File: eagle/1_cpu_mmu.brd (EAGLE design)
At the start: 30 parts, among them IC1 MT5C6408, IC10 74LS157N, IC11 74LS157N, IC12 74LS157N, IC13 74LS157N, IC14 74LS157N, IC15 74LS04N, IC17 74LS32N, IC18 74LS00N, IC19 74LS32N, IC2 MT5C6408, IC20 74LS02N, IC21 74LS374N, IC3 74LS27N, IC4 74LS20N, IC5 74LS08N, IC6 74LS245N, IC7 74LS245N, IC8 74LS32N, IC9 74LS157N

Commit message: Sat Feb  6 20:10:54 CET 2016
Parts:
- removed IC12: 74LS157N, 74xx-eu:DIL16
- added IC16: 74LS08N, 74xx-eu:DIL14
- moved IC7 7.63 mm to (128.3, 40.3)
- moved IC2 1.27 mm to (114.0, 35.2)
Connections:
- removed net /ENMEMX: IC12.4
- removed net /LDMEMX: IC12.7
- removed net N$20: IC12.6, IC17.8
- removed net N$33: IC17.10, IC18.3
- removed net N$39: IC12.1, IC5.8
- new net N$3: IC16.12, IC20.4
- new net N$36: IC16.13, IC5.11
- new net N$38: IC16.11, IC4.13
- net +5V: no longer IC12.11, IC12.14, IC12.2, IC12.5
- net /ENMEM: no longer IC12.3
- net /LDMEM: no longer IC17.9
- net /NP_FAULT: no longer IC12.12
- net /PPREG: no longer IC5.10
- net /PTAB: no longer IC5.9
- net /WR_FAULT: no longer IC12.9
- net ABUS5: now also IC5.12
- net BUSCLKA: now also IC19.9
- net CLK0A: no longer IC19.9
- net GND: now also IC16.7; no longer IC12.15, IC12.8
- net MEMSEG: now also IC5.13
- net N$31: no longer IC12.10
- net N$32: no longer IC12.13
- net N$34: no longer IC18.2
- net N$35: no longer IC18.1
- net VCC: now also IC16.14; no longer IC12.16
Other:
- board text added: "#1"
- board text removed: "#0a"

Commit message: MMU board in progress
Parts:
- removed IC16: 74LS08N, 74xx-eu:DIL14
- removed IC17: 74LS32N, 74xx-eu:DIL14
- removed IC18: 74LS00N, 74xx-eu:DIL14
- added IC12: 74LS00N, 74xx-eu:DIL14
- JP5: device pinhead:2X05 -> pinhead:2X06
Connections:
- removed net N$34: IC17.11, IC17.4
- removed net N$35: IC17.1, IC19.3
- new net /ENMEMX: JP5.11
- new net /LDMEMX: JP5.12
- new net /MEMOP: IC19.1, JP10.11
- new net N$20: IC19.3, IC19.4
- net /ENMEM: no longer IC5.5
- net /FP: no longer IC17.13
- net /LDMEM: no longer IC17.5, IC5.4
- net /PPREG: now also IC12.10
- net /PTAB: now also IC12.9
- net FPRESENT: no longer IC19.1
- net FWRITABLE: no longer IC17.12
- net GND: now also IC12.7; no longer IC16.7, IC17.7, IC18.7
- net N$19: now also IC12.2; no longer IC17.2, IC5.6
- net N$3: now also IC5.9; no longer IC16.12
- net N$31: now also IC12.1; no longer IC17.6, IC18.9
- net N$32: now also IC12.8, IC19.5; no longer IC17.3, IC18.10
- net N$36: now also IC5.10; no longer IC16.13
- net N$38: now also IC5.8; no longer IC16.11
- net N$40: now also IC12.3; no longer IC18.8
- net VCC: now also IC12.14; no longer IC16.14, IC17.14, IC18.14

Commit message: MMU schematics completed
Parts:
- removed IC15: 74LS04N, 74xx-eu:DIL14
- added IC16: 74LS08N, 74xx-eu:DIL14
- added IC17: 74LS32N, 74xx-eu:DIL14
- moved IC3 115.5 mm to (119.4, 17.8), turned to 180 degrees
- moved IC12 107.1 mm to (41.3, 84.8), turned to 270 degrees
- moved IC4 86.7 mm to (91.1, 17.8)
- moved IC9 74.7 mm to (117.8, 45.1), turned to 180 degrees
- moved IC2 69.1 mm to (58.1, 75.9)
- moved IC19 68.3 mm to (23.2, 72.1), turned to 270 degrees
- moved IC5 62.9 mm to (68.6, 17.8)
- moved IC13 61.7 mm to (117.8, 31.4), turned to 180 degrees
- moved IC10 45.6 mm to (89.9, 45.1), turned to 180 degrees
- moved IC7 44.9 mm to (109.9, 81.3)
- moved IC21 43.8 mm to (92.4, 70.8), turned to 90 degrees
- moved IC20 43.7 mm to (44.8, 31.8)
- moved IC1 38.7 mm to (75.2, 75.9)
- moved IC14 33.1 mm to (89.9, 31.4), turned to 180 degrees
- moved IC11 21.0 mm to (64.1, 45.1), turned to 180 degrees
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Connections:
- removed net FIO: IC15.3, IC2.17, IC7.7
- removed net FPRESENT: IC2.19, IC7.9
- removed net FWRITABLE: IC2.18, IC7.8
- removed net N$18: IC11.11, IC15.4
- removed net N$19: IC12.2
- removed net N$31: IC12.1
- new net /FIO: IC11.11, IC2.17, IC7.7
- new net /FPRESENT: IC12.4, IC2.19, IC7.9
- new net /FWRITABLE: IC12.12, IC2.18, IC7.8
- new net N$33: IC12.5, IC20.1, IC5.4
- new net N$34: IC12.13, IC5.6
- net /ENMEM: now also IC17.2, IC5.5
- net /ENMEMX: now also IC17.3
- net /FP: now also IC17.10; no longer IC19.2
- net /LDMEM: now also IC17.5
- net /LDMEMX: now also IC17.6
- net /MEMOP: now also IC17.9; no longer IC19.1
- net /NP_FAULT: now also IC12.6, IC16.4
- net /WR_FAULT: now also IC12.11, IC16.5
- net ABUS0: now also IC12.2; no longer IC15.1
- net GND: now also IC16.7, IC17.7; no longer IC10.6, IC15.7
- net MEMSEG: now also IC10.6
- net N$20: now also IC17.8, IC20.2; no longer IC19.3, IC19.4
- net N$30: now also IC12.3; no longer IC15.2
- net N$32: now also IC17.1, IC17.4, IC20.3; no longer IC19.5
- net N$40: now also IC16.6; no longer IC12.3
- net VCC: now also IC16.14, IC17.14; no longer IC15.14
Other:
- board outline added: 160 x 100 mm

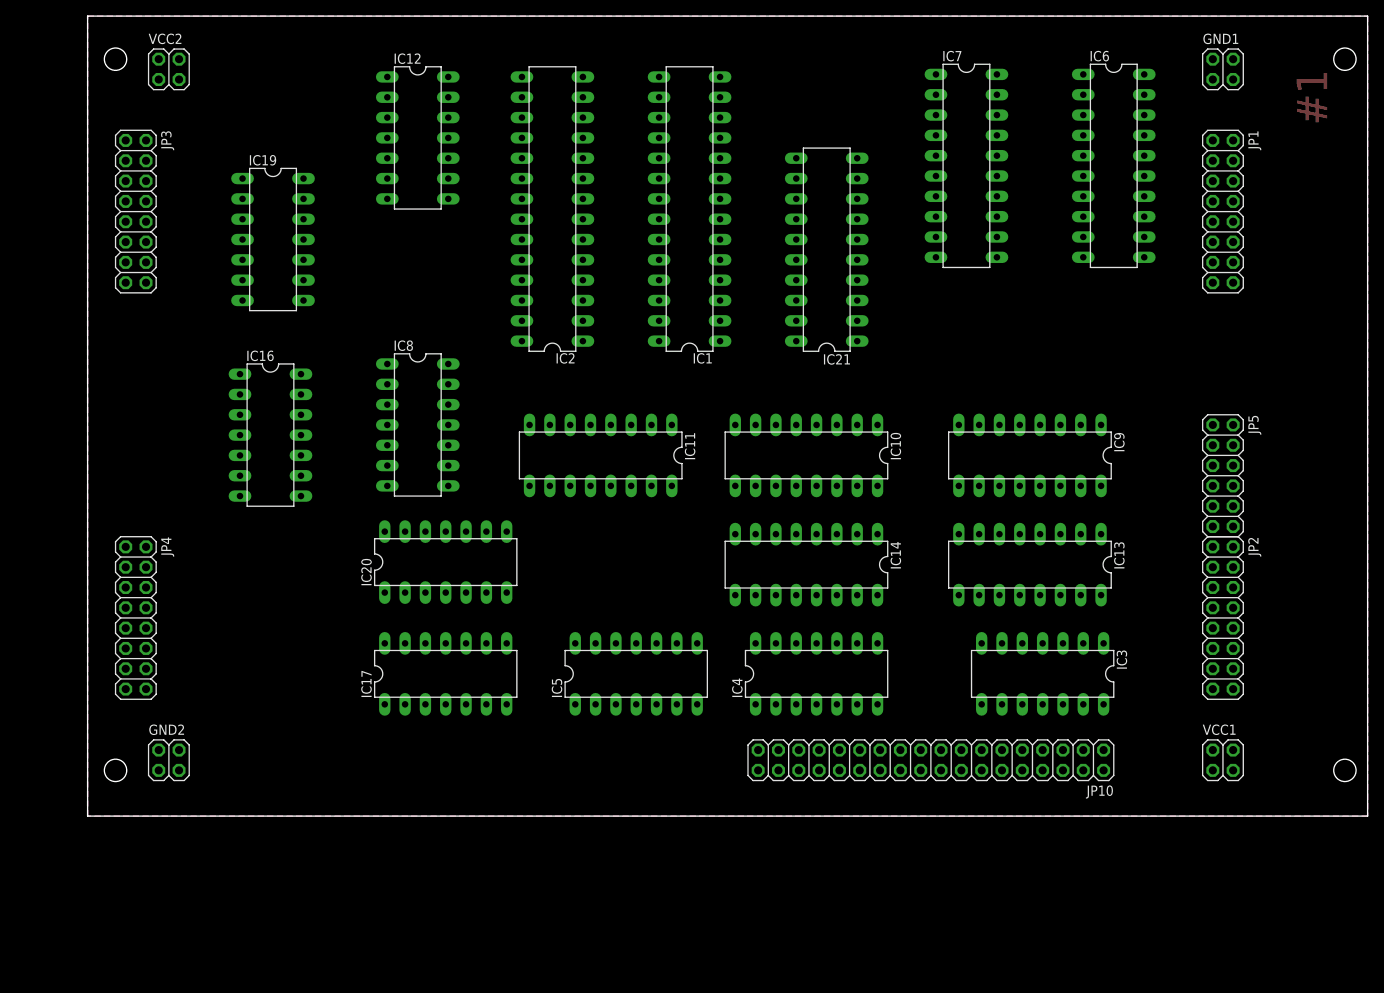
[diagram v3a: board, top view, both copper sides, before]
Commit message: MMU power rails and bypass caps added in schematic, board started
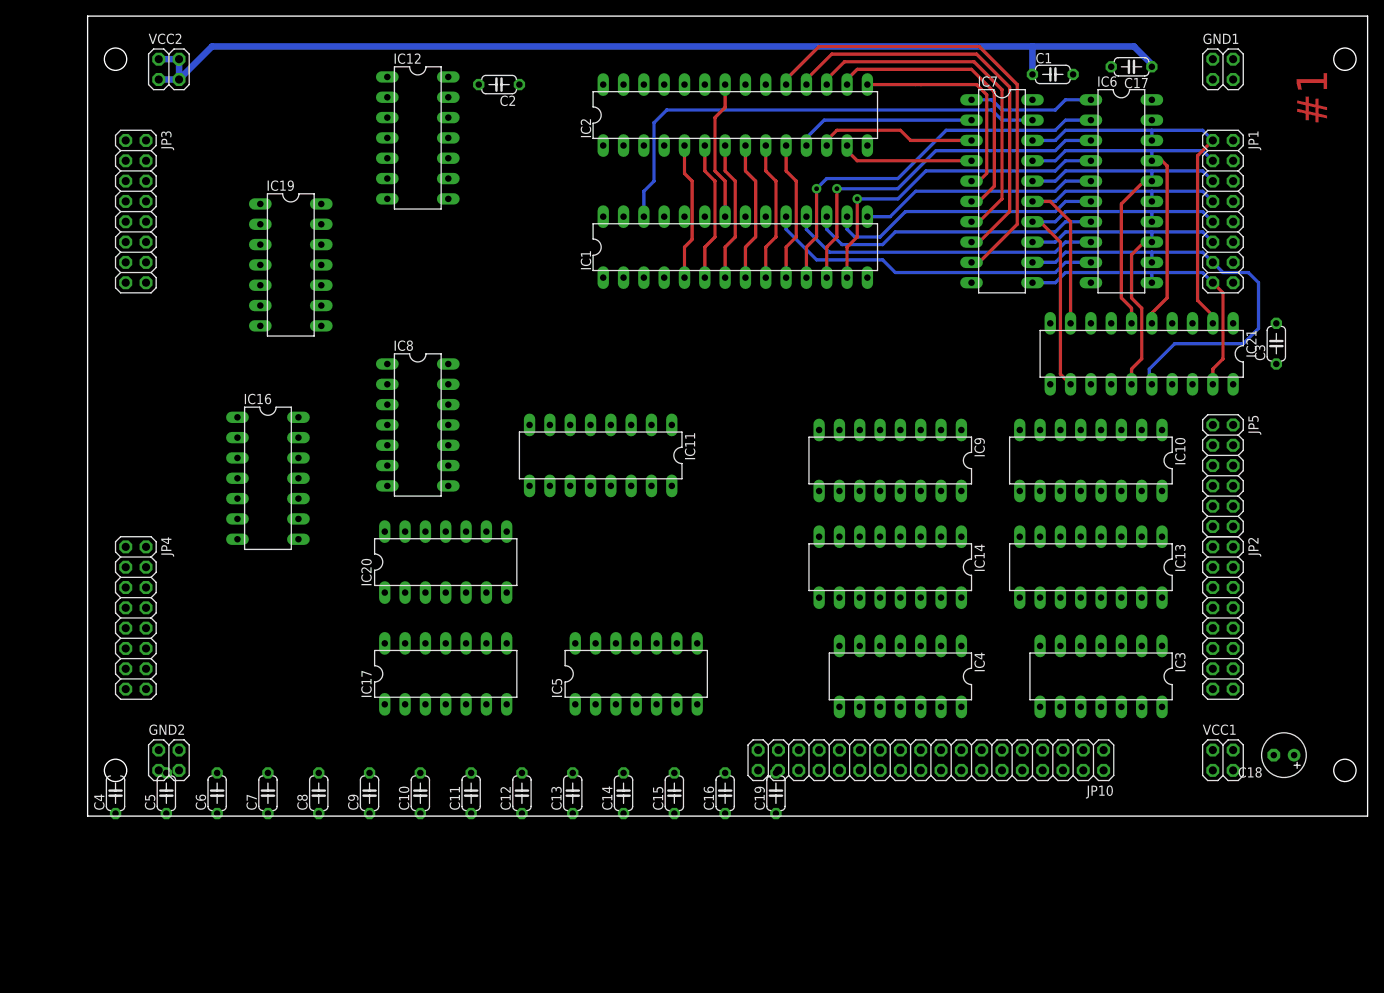
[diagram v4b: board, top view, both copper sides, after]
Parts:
- added C1, C10, C11, C12, C13, C14, C15, C16, C17, C19, C2, C3, C4, C5, C6, C7, C8, C9: 100n, rcl:C050-024X044
- added C18: 10u, rcl:E2,5-6
- moved IC21 41.5 mm to (131.8, 57.8), turned to 180 degrees
- moved IC10 35.6 mm to (125.4, 44.5)
- moved IC2 25.7 mm to (81.0, 87.6), turned to 0 degrees
- moved IC9 17.5 mm to (100.3, 44.5)
- moved IC14 10.5 mm to (100.3, 31.1)
- moved IC4 10.5 mm to (101.6, 17.5), turned to 180 degrees
- moved IC13 7.63 mm to (125.4, 31.1)
- moved IC1 7.44 mm to (81.0, 71.1), turned to 0 degrees
- moved IC3 7.31 mm to (126.7, 17.5)
- moved IC7 5.46 mm to (114.3, 78.1)
- moved IC16 5.41 mm to (22.5, 42.2)
- moved IC19 3.88 mm to (25.4, 68.9)
- moved IC6 3.31 mm to (129.2, 78.1)
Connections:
- net +5V: now also C1.1, C10.1, C11.1, C12.1, C13.1, C14.1, C15.1, C16.1, C17.1, C18.+, C19.1, C2.1, C3.1, C4.1, C5.1, C6.1, C7.1, C8.1, C9.1, IC1.28, IC10.16, IC11.16, IC12.14, IC13.16, IC14.16, IC16.14, IC17.14, IC19.14, IC2.28, IC20.14, IC21.20, IC3.14, IC4.14, IC5.14, IC6.20, IC7.20, IC9.16
- net GND: now also C1.2, C10.2, C11.2, C12.2, C13.2, C14.2, C15.2, C16.2, C17.2, C18.-, C19.2, C2.2, C3.2, C4.2, C5.2, C6.2, C7.2, C8.2, C9.2, IC16.1, IC16.10, IC16.12, IC16.13, IC16.2, IC16.9, IC17.12, IC17.13, IC19.1, IC19.2, IC19.4, IC19.5, IC20.11, IC20.12, IC20.8, IC20.9
- net VCC: no longer IC1.28, IC10.16, IC11.16, IC12.14, IC13.16, IC14.16, IC16.14, IC17.14, IC19.14, IC2.28, IC20.14, IC21.20, IC3.14, IC4.14, IC5.14, IC6.20, IC7.20, IC9.16
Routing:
- net +5V: track 0.00 -> 135.7 mm
- net N$27: track 0.00 -> 60.8 mm
- net /FPRESENT: track 0.00 -> 58.4 mm
- net DBUS6: track 0.00 -> 55.1 mm
- net /FWRITABLE: track 0.00 -> 51.0 mm
- net N$5: track 0.00 -> 49.5 mm, vias 0 -> 1
- net DBUS0: track 0.00 -> 49.3 mm
- net DBUS4: track 0.00 -> 47.7 mm
- net DBUS1: track 0.00 -> 47.5 mm
- net N$6: track 0.00 -> 45.9 mm, vias 0 -> 1
- net DBUS2: track 0.00 -> 45.3 mm
- net DBUS5: track 0.00 -> 45.3 mm
- net /FIO: track 0.00 -> 43.6 mm
- net DBUS3: track 0.00 -> 43.4 mm
- net N$12: track 0.00 -> 42.4 mm
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- removed copper zone on layer 1, net GND
- removed copper zone on layer 16, net GND

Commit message: MMU board layout updates
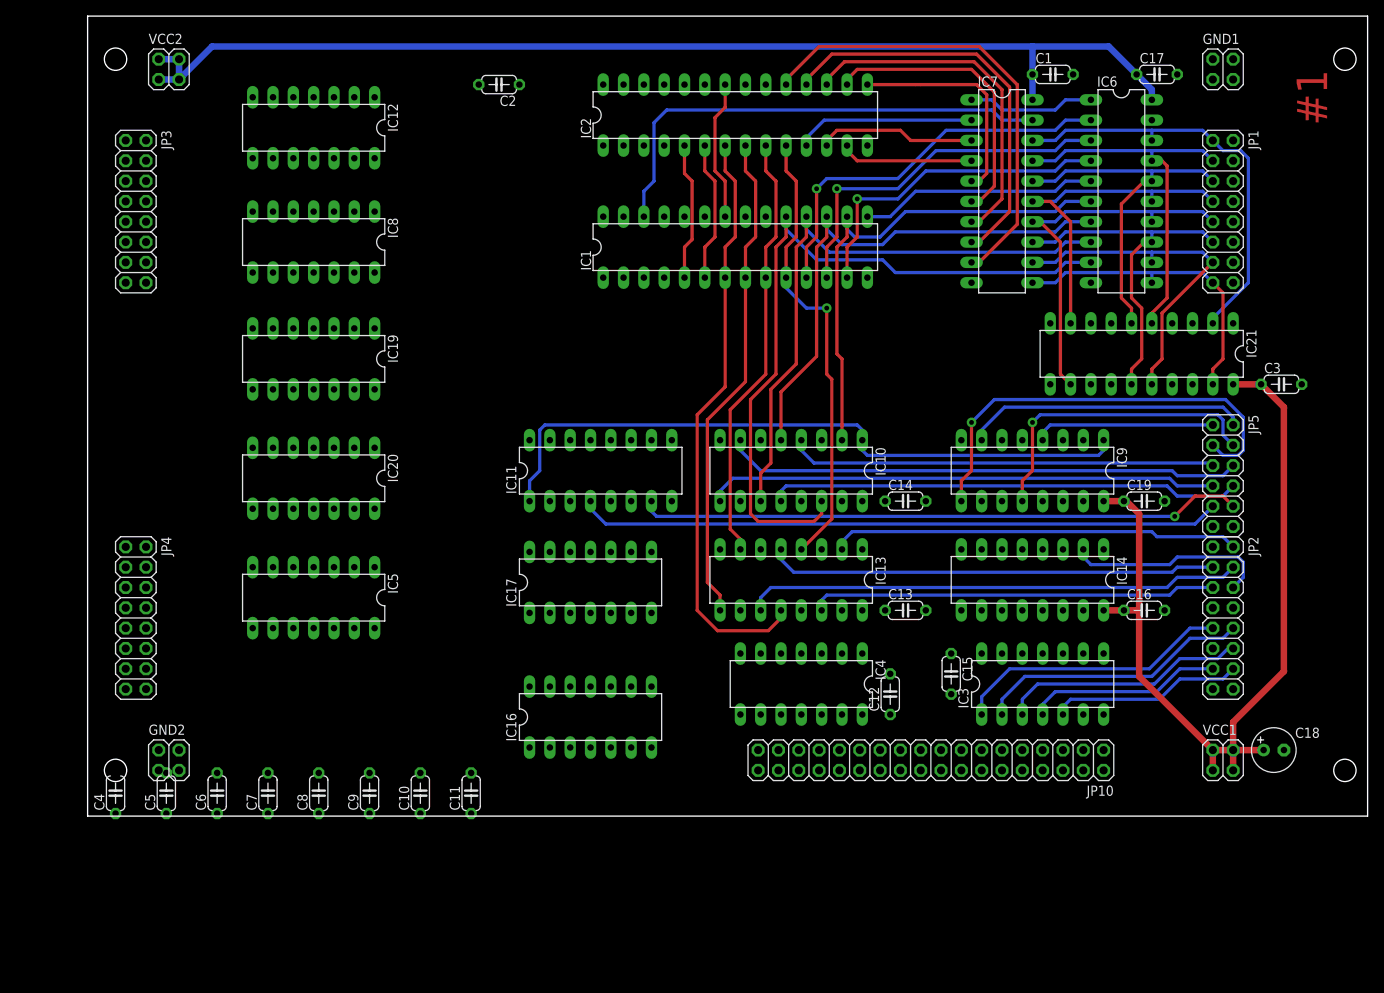
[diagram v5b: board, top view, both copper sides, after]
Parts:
- moved C19 58.8 mm to (132.1, 39.4), turned to 0 degrees
- moved C16 57.2 mm to (132.1, 25.7), turned to 0 degrees
- moved C14 50.7 mm to (102.2, 39.4), turned to 0 degrees
- moved IC16 50.2 mm to (62.9, 12.4), turned to 0 degrees
- moved C12 47.7 mm to (100.3, 15.2)
- moved C13 47.5 mm to (102.2, 25.7), turned to 0 degrees
- moved IC5 41.4 mm to (28.3, 27.3), turned to 180 degrees
- moved C15 37.7 mm to (108.0, 17.8), turned to 270 degrees
- moved IC13 37.5 mm to (87.9, 29.5)
- moved IC10 37.5 mm to (87.9, 43.2)
- moved IC8 26.3 mm to (28.3, 71.8), turned to 180 degrees
- moved IC17 21.4 mm to (62.9, 29.2)
- moved IC20 19.6 mm to (28.3, 42.2), turned to 180 degrees
- moved IC14 17.9 mm to (118.1, 29.5)
- moved IC9 17.8 mm to (118.1, 43.2)
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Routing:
- net +5V: track 135.7 -> 248.5 mm
- net /FP: track 0.00 -> 84.8 mm
- net PABUS20: track 0.00 -> 80.4 mm
- net PABUS21: track 0.00 -> 75.8 mm, vias 0 -> 1
- net PABUS17: track 0.00 -> 64.7 mm
- net PABUS18: track 0.00 -> 63.9 mm
- net ABUS3: track 0.00 -> 62.2 mm
- net PABUS19: track 0.00 -> 59.1 mm
- net N$24: track 17.6 -> 73.7 mm
- net ABUS2: track 0.00 -> 56.2 mm
- net PABUS14: track 0.00 -> 55.2 mm, vias 0 -> 1
- net PABUS16: track 0.00 -> 53.5 mm
- net ABUS1: track 0.00 -> 51.2 mm
- net ABUS4: track 0.00 -> 50.8 mm
- net N$12: track 42.4 -> 92.7 mm
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
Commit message: MMU board updates 2016-02-24
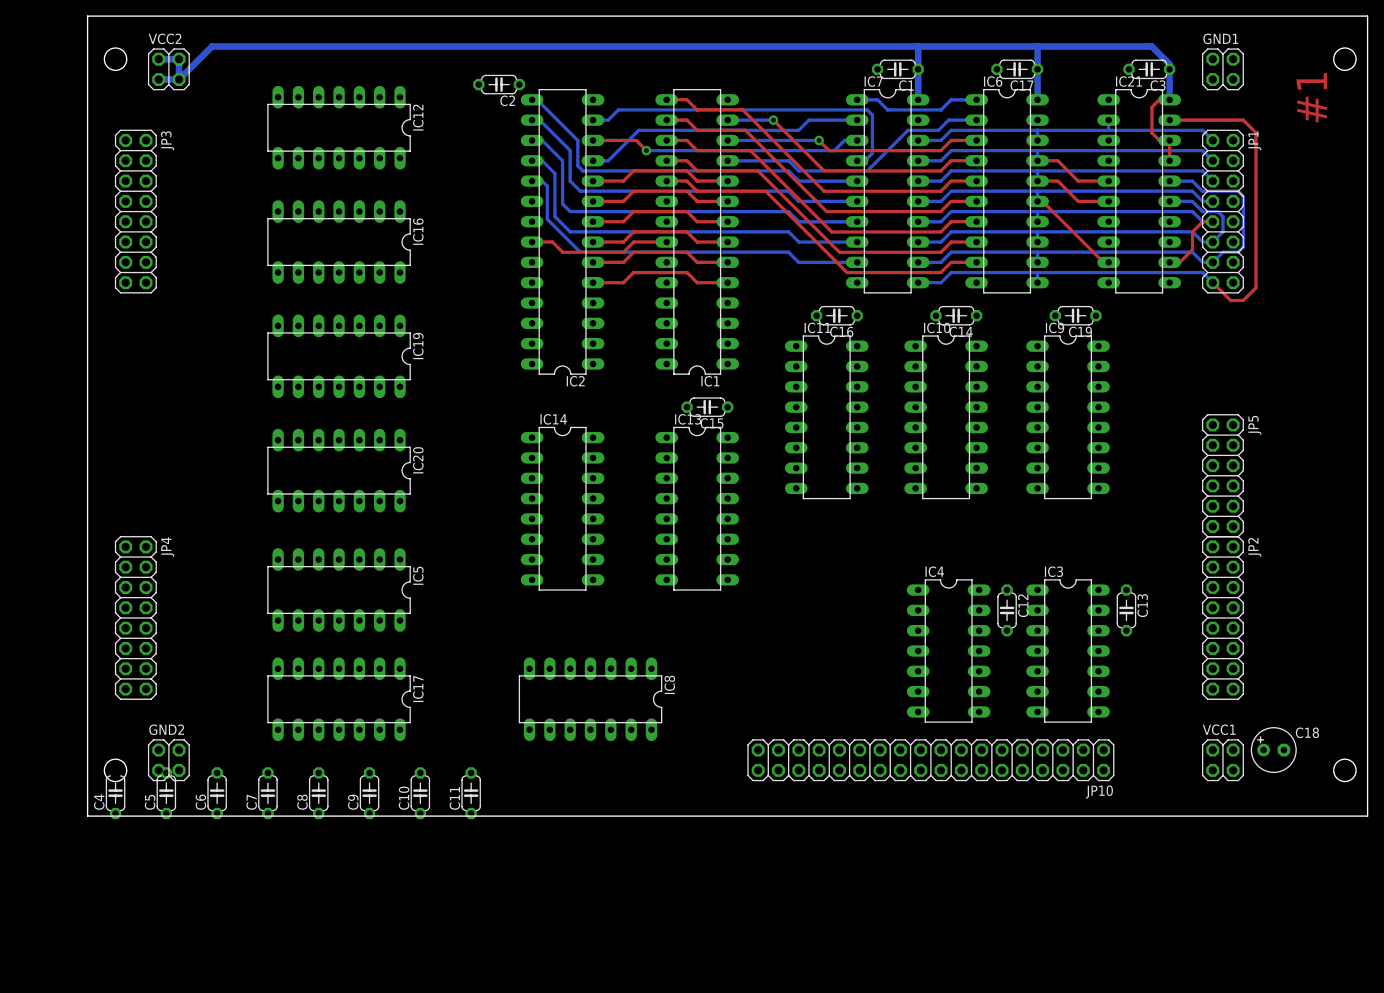
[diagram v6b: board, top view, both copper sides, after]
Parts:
- moved IC16 67.2 mm to (31.4, 71.8), turned to 180 degrees
- moved IC8 66.8 mm to (62.9, 14.6)
- moved IC14 59.4 mm to (59.4, 38.4), turned to 270 degrees
- moved C16 53.2 mm to (93.7, 62.5), turned to 180 degrees
- moved C15 45.2 mm to (77.5, 51.1), turned to 180 degrees
- moved C3 42.7 mm to (132.7, 93.3), turned to 180 degrees
- moved IC17 34.7 mm to (31.4, 14.6), turned to 180 degrees
- moved IC11 29.0 mm to (92.4, 49.8), turned to 270 degrees
- moved C13 27.6 mm to (129.9, 25.7), turned to 270 degrees
- moved IC2 26.1 mm to (59.4, 73.0), turned to 90 degrees
- moved C19 24.7 mm to (123.5, 62.5), turned to 180 degrees
- moved C14 24.0 mm to (108.6, 62.5), turned to 180 degrees
- moved IC10 20.5 mm to (107.3, 49.8), turned to 270 degrees
- moved IC21 20.3 mm to (131.4, 78.1), turned to 270 degrees
- moved C1 19.4 mm to (101.3, 93.3), turned to 180 degrees
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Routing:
- net +5V: track 248.5 -> 162.8 mm
- net /FP: track 84.8 -> 0.00 mm
- net PABUS20: track 80.4 -> 0.00 mm
- net PABUS21: track 75.8 -> 0.00 mm, vias 1 -> 0
- net PABUS17: track 64.7 -> 0.00 mm
- net PABUS18: track 63.9 -> 0.00 mm
- net ABUS3: track 62.2 -> 0.00 mm
- net N$27: track 60.8 -> 0.00 mm
- net PABUS19: track 59.1 -> 0.00 mm
- net ABUS2: track 56.2 -> 0.00 mm
- net N$24: track 73.7 -> 17.9 mm
- net PABUS14: track 55.2 -> 0.00 mm, vias 1 -> 0
- net PABUS16: track 53.5 -> 0.00 mm
- net ABUS1: track 51.2 -> 0.00 mm
- net ABUS4: track 50.8 -> 0.00 mm
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
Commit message: MMU board updates 2016-02-25
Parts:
- added C20: 100n, rcl:C050-024X044
- moved IC17 59.7 mm to (90.8, 21.0), turned to 270 degrees
- moved C12 9.72 mm to (107.3, 31.8), turned to 180 degrees
- moved C13 8.53 mm to (123.8, 31.8), turned to 180 degrees
- moved IC4 1.62 mm to (106.0, 21.0)
- moved C14 1.14 mm to (107.6, 61.9)
- moved C16 0.63 mm to (93.7, 61.9)
- moved C19 0.63 mm to (123.5, 61.9)
- moved IC3 0.32 mm to (122.6, 21.0)
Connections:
- removed net VCC: IC8.14
- net +5V: now also C20.1, IC8.14
- net GND: now also C20.2
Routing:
- net MEMSEG: track 0.00 -> 147.2 mm
- net ABUS12: track 0.00 -> 112.7 mm
- net ABUS13: track 0.00 -> 107.6 mm
- net ABUS15: track 0.00 -> 101.2 mm, vias 0 -> 2
- net ABUS14: track 0.00 -> 99.5 mm
- net PABUS20: track 0.00 -> 68.6 mm
- net /FS: track 0.00 -> 65.1 mm
- net PABUS21: track 0.00 -> 57.6 mm
- net N$7: track 34.3 -> 82.4 mm
- net PABUS16: track 0.00 -> 41.5 mm
- net PABUS17: track 0.00 -> 40.9 mm
- net N$6: track 32.2 -> 72.7 mm
- net N$8: track 44.0 -> 83.7 mm, vias 0 -> 1
- net PABUS19: track 0.00 -> 38.7 mm
- net N$5: track 34.3 -> 69.7 mm
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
